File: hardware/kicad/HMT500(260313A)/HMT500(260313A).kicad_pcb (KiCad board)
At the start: 4 copper layers, 56.5 x 23 mm, 104 parts, among them J1 SM08B-GHS-TB, J2 TC2030-IDC-NL, J3 SM04B-SRSS-TB, J5 CHASSIS wire, Q1 MMBTA06, U1 TPS26600PWPR, U10 TPS26611DDFR, U11 THVD2410DGKR, U12 OPA197IDBVR, U13 OPA197IDBVR, U14 SN74LVC2G32DCUR, U2 LMR36006BRNXR, U3 TPS7A2033PDBVR, U4 STM32G0B1CCT3, U5 PCAP04-AQFM-24, U6 ADS1220IPWR, U7 DAC8760IPWP, U8 DAC8760IPWP, U9 TPS26611DDFR

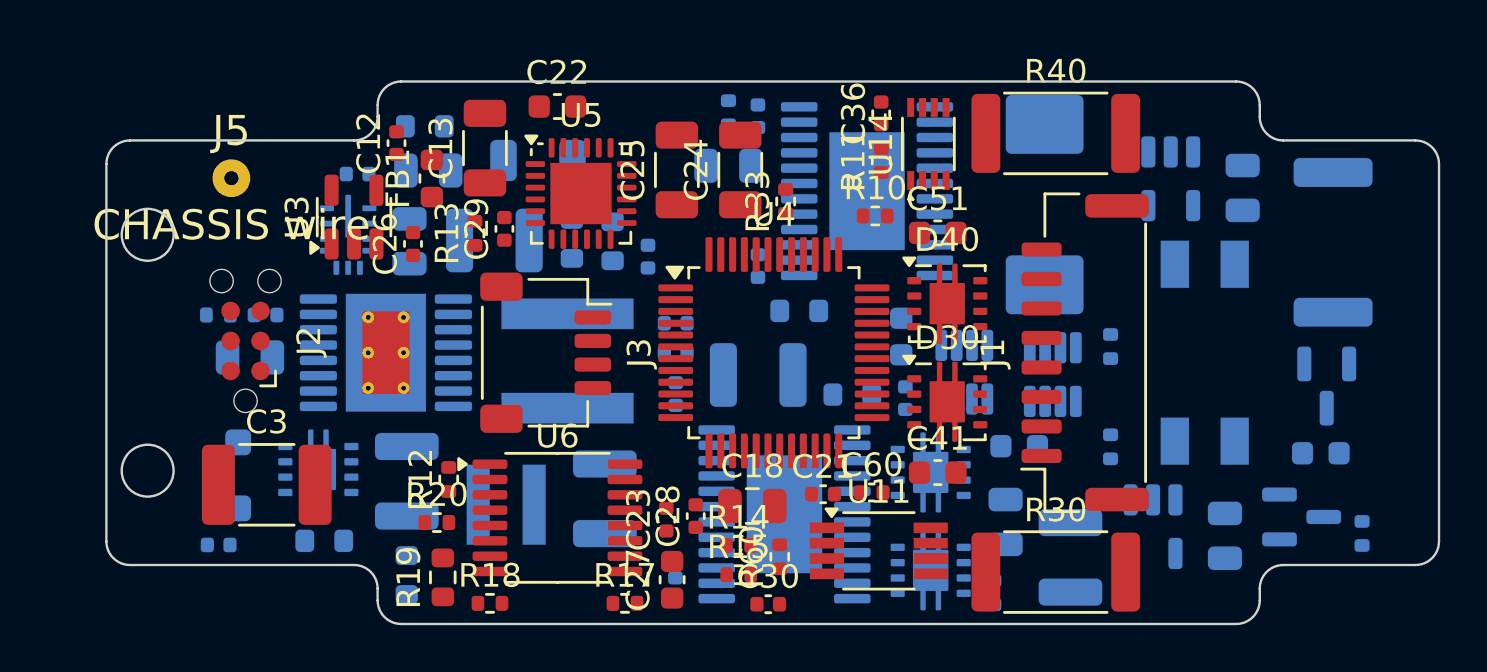
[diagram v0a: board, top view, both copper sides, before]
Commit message: Decision #37: fix the DAC section with the IVS320 AO rev 1.0 scheme
- AO supply VAO 16.1 V: LMR51606YFDBVR buck (U15) + 22 uH + 2x10 uF,
  feeding DAC AVDD (via 10 ohm), TPS26611 +Vs and OPA197 V+
- Remove +Vs zener follower (Q1, R50, D50, C53) and C43
- DAC CMP compensation 4.7 nF VOUT-CMP + 100 pF CMP-GND (SBAS528D 8.3.2)
- DAC output clamp BAS70-04 (D41/D51) for protector switching transients
- Output TVS3301 and SGOOD -> MCU ADC kept (+-30 V miswiring requirement)
- 114/114 parts placed, netlist 82/82, DRC no clearance errors,
  assembly sim 23 OK; parts list, JLC BOM, review docs updated

Co-Authored-By: Claude Opus 5.5 <noreply@anthropic.com>
Claude-Session: https://claude.ai/code/session_01JA2o8uJsqp9Vzsg4b665ev
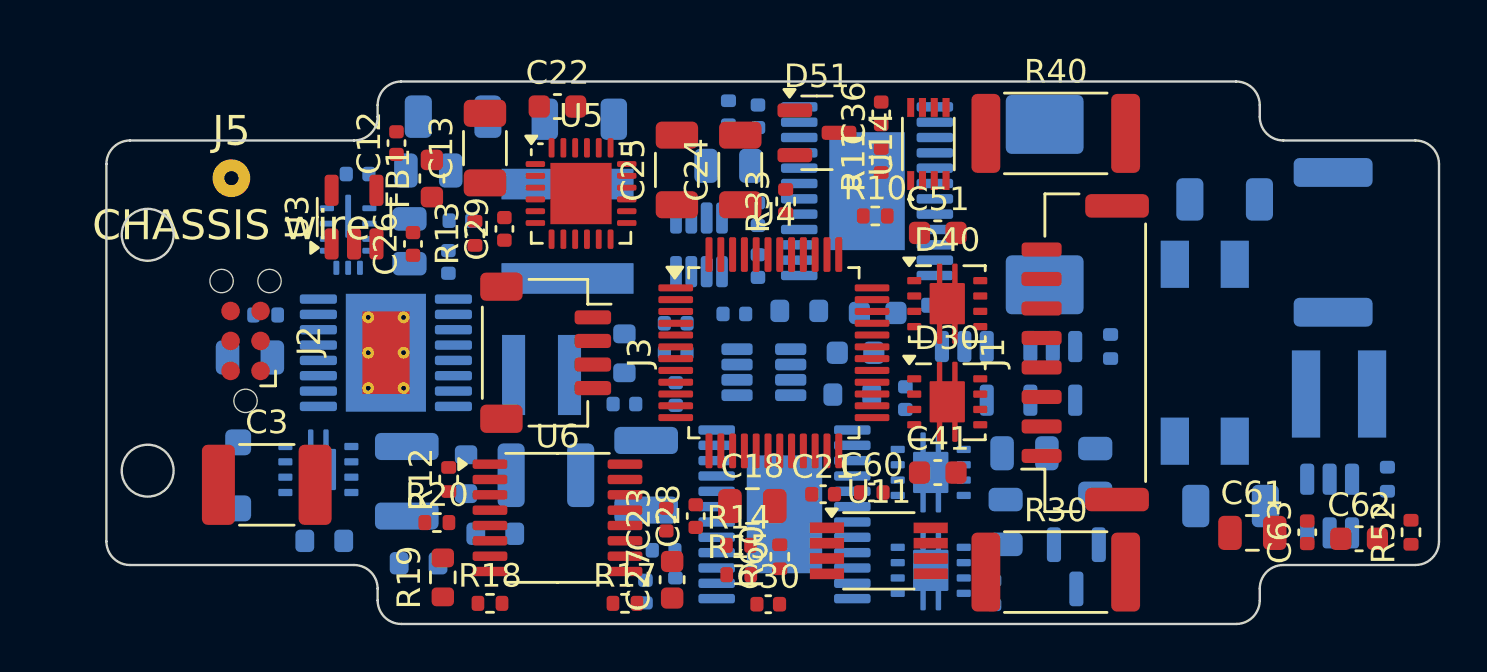
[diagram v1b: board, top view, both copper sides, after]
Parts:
- removed C43: 4.7u 50V, Capacitor_SMD:C_1210_3225Metric
- removed C53: 100n/50V, Capacitor_SMD:C_0603_1608Metric
- removed D50: BZX84C24, Package_TO_SOT_SMD:SOT-23
- removed Q1: MMBTA06, Package_TO_SOT_SMD:SOT-23
- removed R50: 10k, Resistor_SMD:R_0402_1005Metric
- added C47: 4.7n, Capacitor_SMD:C_0402_1005Metric, B.Cu at (123.6, 108.4)
- added C48: 100p C0G, Capacitor_SMD:C_0402_1005Metric, B.Cu at (122.9, 110.1)
- added C57: 4.7n, Capacitor_SMD:C_0402_1005Metric, B.Cu at (127.6, 94.1)
- added C58: 100p C0G, Capacitor_SMD:C_0402_1005Metric, B.Cu at (126.6, 98.4)
- added C61: 2.2u 50V, Capacitor_SMD:C_0805_2012Metric, F.Cu at (148.6, 107.6)
- added C62: 100n/50V, Capacitor_SMD:C_0603_1608Metric, F.Cu at (153.1, 107.9)
- added C63: 100n, Capacitor_SMD:C_0402_1005Metric, F.Cu at (150.9, 107.6)
- added C64: 10u 50V, Capacitor_SMD:C_1206_3216Metric, B.Cu at (147.7, 106.5)
- added C65: 10u 50V, Capacitor_SMD:C_1206_3216Metric, B.Cu at (147.4, 93.5)
- added D41: BAS70-04, Package_TO_SOT_SMD:SOT-23, B.Cu at (141.1, 109.1)
- added D51: BAS70-04, Package_TO_SOT_SMD:SOT-23, F.Cu at (130.1, 90.7)
- added L3: 22uH, Inductor_SMD:L_Taiyo-Yuden_NR-40xx, B.Cu at (152.3, 101.8)
- added R51: 422k 1%, Resistor_SMD:R_0402_1005Metric, B.Cu at (154.3, 105.4)
- added R52: 22.1k 1%, Resistor_SMD:R_0402_1005Metric, F.Cu at (155.3, 107.6)
- added U15: LMR51606YFDBVR, Package_TO_SOT_SMD:SOT-23-6, B.Cu at (151.9, 106.5)
- C5: footprint Capacitor_SMD:C_1210_3225Metric -> Capacitor_SMD:C_1206_3216Metric
- moved C11 17.2 mm to (115.0, 94.4)
- moved U10 16.0 mm to (125.1, 95.4)
- moved R9 14.9 mm to (115.2, 105.2), turned to -90 degrees
- moved C55 13.5 mm to (141.9, 105.0)
- moved R5 12.9 mm to (116.5, 107.7), turned to 0 degrees
- moved U12 10.3 mm to (136.4, 100.9)
- moved C6 9.95 mm to (118.6, 105.2)
- moved U13 9.65 mm to (140.1, 100.9)
- moved R31 9.41 mm to (135.3, 98.0), turned to 0 degrees
- moved C45 9.19 mm to (138.9, 104.3), turned to 0 degrees
- moved U9 8.50 mm to (127.9, 100.8), turned to 0 degrees
- moved C9 8.07 mm to (114.5, 96.2), turned to -90 degrees
- moved C46 7.99 mm to (131.8, 100.0)
- moved C4 6.33 mm to (122.0, 102.2), turned to 0 degrees
- moved L2 5.70 mm to (118.5, 100.9)
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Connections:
- C46 pad 1: VS_CLAMP -> VAO
- C56 pad 1: VS_CLAMP -> VAO
- R34 pad 1: VIN_P -> VAO
- R44 pad 1: VIN_P -> VAO
- U10 pad 6: VS_CLAMP -> VAO
- U7 pad 17: (no net) -> DAC1_CMP
- U8 pad 17: (no net) -> DAC2_CMP
- U9 pad 6: VS_CLAMP -> VAO

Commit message: Decision #38: prefer JLCPCB parts - U2 LMR51606, R19 0.1 %, std 2512
- 5 V buck U2: LMR36006BRNXR -> LMR51606YFDBVR (same IC as VAO buck),
  L2 10 uH, C6 22 uF, R8/R9 118k/22.1k -> 5.07 V; C9, C10, C11, C17 removed
- R19 -> ERA-3AEB4021V (0.1 %, 25 ppm); R1/R30/R40 -> CRCW2512 standard
- LCSC numbers for 422k and 118k; 57 of 60 BOM lines have LCSC numbers
- 110/110 placed, netlist 81/81, DRC no clearance errors, assembly sim OK

Co-Authored-By: Claude Opus 5.5 <noreply@anthropic.com>
Claude-Session: https://claude.ai/code/session_01JA2o8uJsqp9Vzsg4b665ev
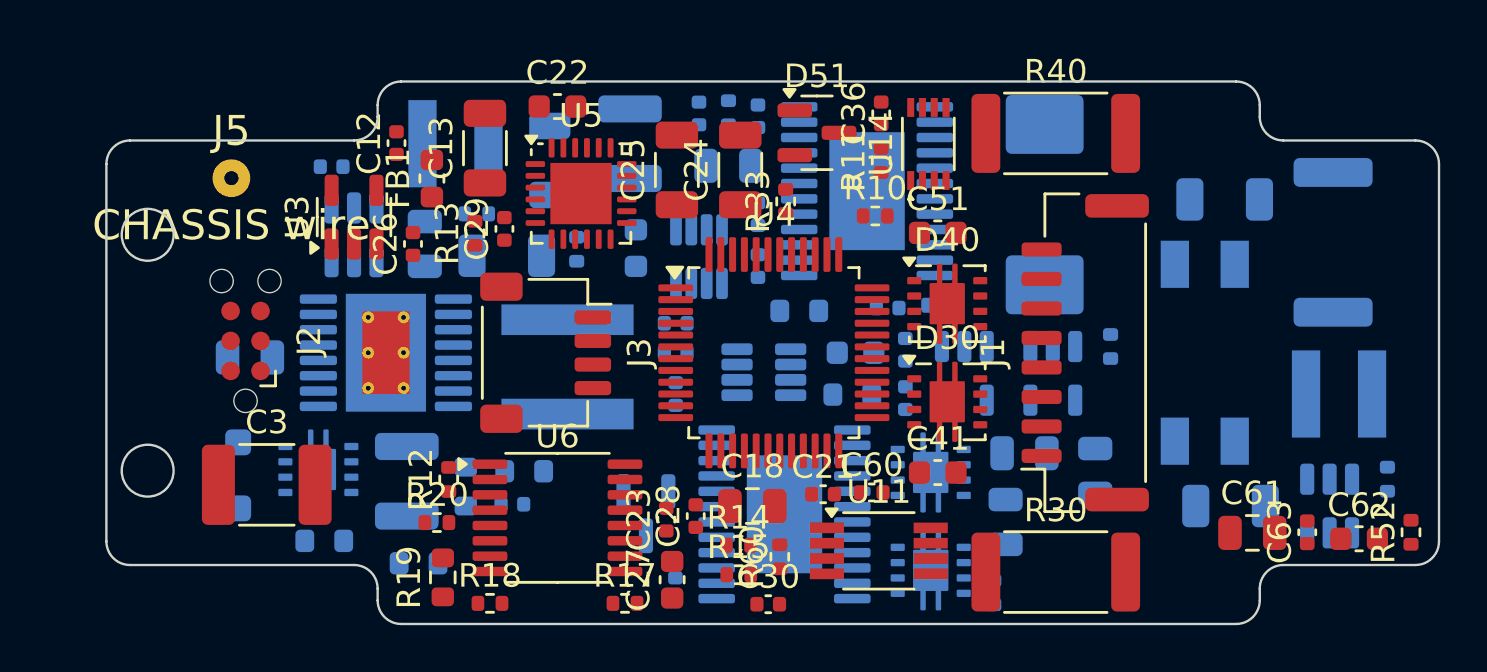
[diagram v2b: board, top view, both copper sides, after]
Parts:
- removed C10: 22u 25V, Capacitor_SMD:C_1210_3225Metric
- removed C11: 20p C0G, Capacitor_SMD:C_0402_1005Metric
- removed C17: 220n 100V, Capacitor_SMD:C_0805_2012Metric
- removed C9: 1u, Capacitor_SMD:C_0402_1005Metric
- L2: value 15uH -> 10uH; footprint Inductor_SMD:L_Coilcraft_XAL4040-XXX -> Inductor_SMD:L_Taiyo-Yuden_NR-40xx
- R8: value 100k 1% -> 118k 1%
- R9: value 24.9k 1% -> 22.1k 1%; footprint Resistor_SMD:R_0603_1608Metric -> Resistor_SMD:R_0402_1005Metric
- U2: value LMR36006BRNXR -> LMR51606YFDBVR; footprint HMT500_260313A:Texas_RNX0012A_VQFN-HR-12_2x3mm -> Package_TO_SOT_SMD:SOT-23-6
- moved D41 18.4 mm to (122.9, 106.8)
- moved C48 15.8 mm to (133.1, 98.1), turned to 0 degrees
- moved C6 14.5 mm to (122.2, 91.1), turned to -90 degrees
- moved R8 13.5 mm to (119.9, 95.6), turned to -90 degrees
- moved C47 13.3 mm to (133.9, 99.9), turned to -90 degrees
- moved R9 11.0 mm to (115.7, 94.1), turned to 0 degrees
- moved C56 10.6 mm to (122.5, 95.6), turned to -90 degrees
- moved L2 10.5 mm to (114.8, 91.1)
- moved C58 8.63 mm to (125.1, 89.9), turned to -90 degrees
- moved R6 6.56 mm to (117.7, 105.0), turned to 0 degrees
- moved C4 6.37 mm to (117.2, 106.4)
- moved C5 6.32 mm to (117.0, 95.9)
- moved GDT1 5.75 mm to (119.5, 100.6)
- moved R4 3.82 mm to (115.2, 105.7), turned to -90 degrees
- moved R5 3.48 mm to (113.2, 108.9)
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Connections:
- C8 pad 1: BUCK_SW -> BUCK_BOOT
- C8 pad 2: BUCK_BOOT -> BUCK_SW
- U2 pad 1: GND -> BUCK_BOOT
- U2 pad 2: VIN_P -> GND
- U2 pad 3: BUCK_SW -> BUCK_FB
- U2 pad 4: BUCK_BOOT -> VIN_P
- U2 pad 5: BUCK_VCC -> VIN_P
- U2 pad 6: GND -> BUCK_SW

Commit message: Decision #39: sample stage uses JLCPCB parts - MCU STM32G0B1CCT6
Same die and pinout as CCT3 (85 C grade); revisit for production once the
electronics temperature spec is set. 58 of 60 BOM lines have LCSC numbers.

Co-Authored-By: Claude Opus 5.5 <noreply@anthropic.com>
Claude-Session: https://claude.ai/code/session_01JA2o8uJsqp9Vzsg4b665ev
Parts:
- U4: value STM32G0B1CCT3 -> STM32G0B1CCT6
